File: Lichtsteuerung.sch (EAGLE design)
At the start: 154 parts, among them IC1 74HC595D, IC10 TSR_1-2450, IC11 MEGA64-A, IC12 75176AD, IC13 DS1307SO8, IC2 74HC595D, IC3 74HC595D, IC4 74HC595D, IC5 75176AD, IC6 MEGA8-AI, IC9 24FC128-I/SN, Q1 32.768, Q2 16MHz, Q3 16MHz, U1 MAX232SOIC16, X1 713-1410, X2 713-1410, X3 733-333, X5 713-1410, X6 733-334, X7 733-333, X8 733-333

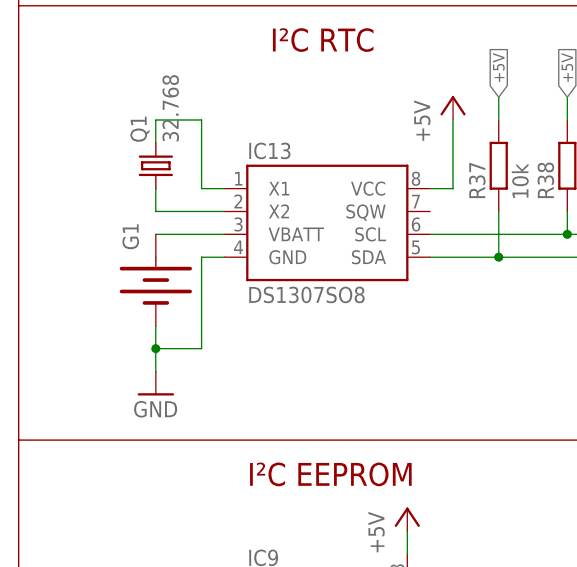
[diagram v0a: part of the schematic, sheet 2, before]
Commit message: Changed CR2032 battery holder with a vertical one to allow easier replacements
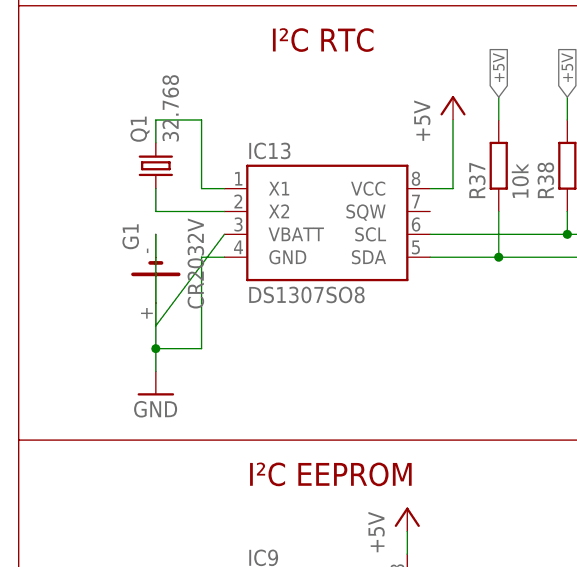
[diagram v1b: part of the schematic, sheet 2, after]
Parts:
- G1: value (none) -> CR2032V; device SparkFun:BATTERY20PTH -> cr2032v2:CR2032V
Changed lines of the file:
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@@
 <part name="FRAME3" library="frames" deviceset="A3L-LOC" device=""/>
 <part name="IC13" library="SparkFun" deviceset="DS1307" device="SO8"/>
-<part name="G1" library="SparkFun" deviceset="BATTERY" device="20PTH"/>
+<part name="G1" library="cr2032v2" deviceset="CR2032V" device=""/>
 <part name="Q1" library="crystal" deviceset="MC-306" device="" value="32.768"/>
 <part name="R37" library="resistor" deviceset="R-EU_" device="R0805" value="10k"/>
@@
 <instance part="FRAME3" gate="G$1" x="0" y="0"/>
 <instance part="IC13" gate="G$1" x="43.18" y="147.32"/>
-<instance part="G1" gate="G$1" x="25.4" y="139.7" smashed="yes" rot="R270">
+<instance part="G1" gate="1" x="25.4" y="139.7" smashed="yes" rot="R270">
 <attribute name="NAME" x="23.495" y="143.002" size="1.778" layer="95" rot="R90"/>
 <attribute name="VALUE" x="28.956" y="146.558" size="1.778" layer="96" rot="R270"/>
@@
 <net name="N$40" class="0">
 <segment>
-<wire x1="25.4" y1="144.78" x2="33.02" y2="144.78" width="0.1524" layer="91"/>
-<pinref part="G1" gate="G$1" pin="+"/>
+<wire x1="25.4" y1="134.62" x2="33.02" y2="144.78" width="0.1524" layer="91"/>
+<pinref part="G1" gate="1" pin="+"/>
 <pinref part="IC13" gate="G$1" pin="VBATT"/>
 </segment>
@@
 </segment>
 <segment>
-<wire x1="25.4" y1="134.62" x2="25.4" y2="132.08" width="0.1524" layer="91"/>
+<wire x1="25.4" y1="144.78" x2="25.4" y2="132.08" width="0.1524" layer="91"/>
 <wire x1="25.4" y1="132.08" x2="30.48" y2="132.08" width="0.1524" layer="91"/>
 <wire x1="30.48" y1="132.08" x2="30.48" y2="142.24" width="0.1524" layer="91"/>
@@
 <wire x1="25.4" y1="129.54" x2="25.4" y2="132.08" width="0.1524" layer="91"/>
 <junction x="25.4" y="132.08"/>
-<pinref part="G1" gate="G$1" pin="-"/>
+<pinref part="G1" gate="1" pin="-"/>
 <pinref part="IC13" gate="G$1" pin="GND"/>
 <pinref part="GND21" gate="1" pin="GND"/>

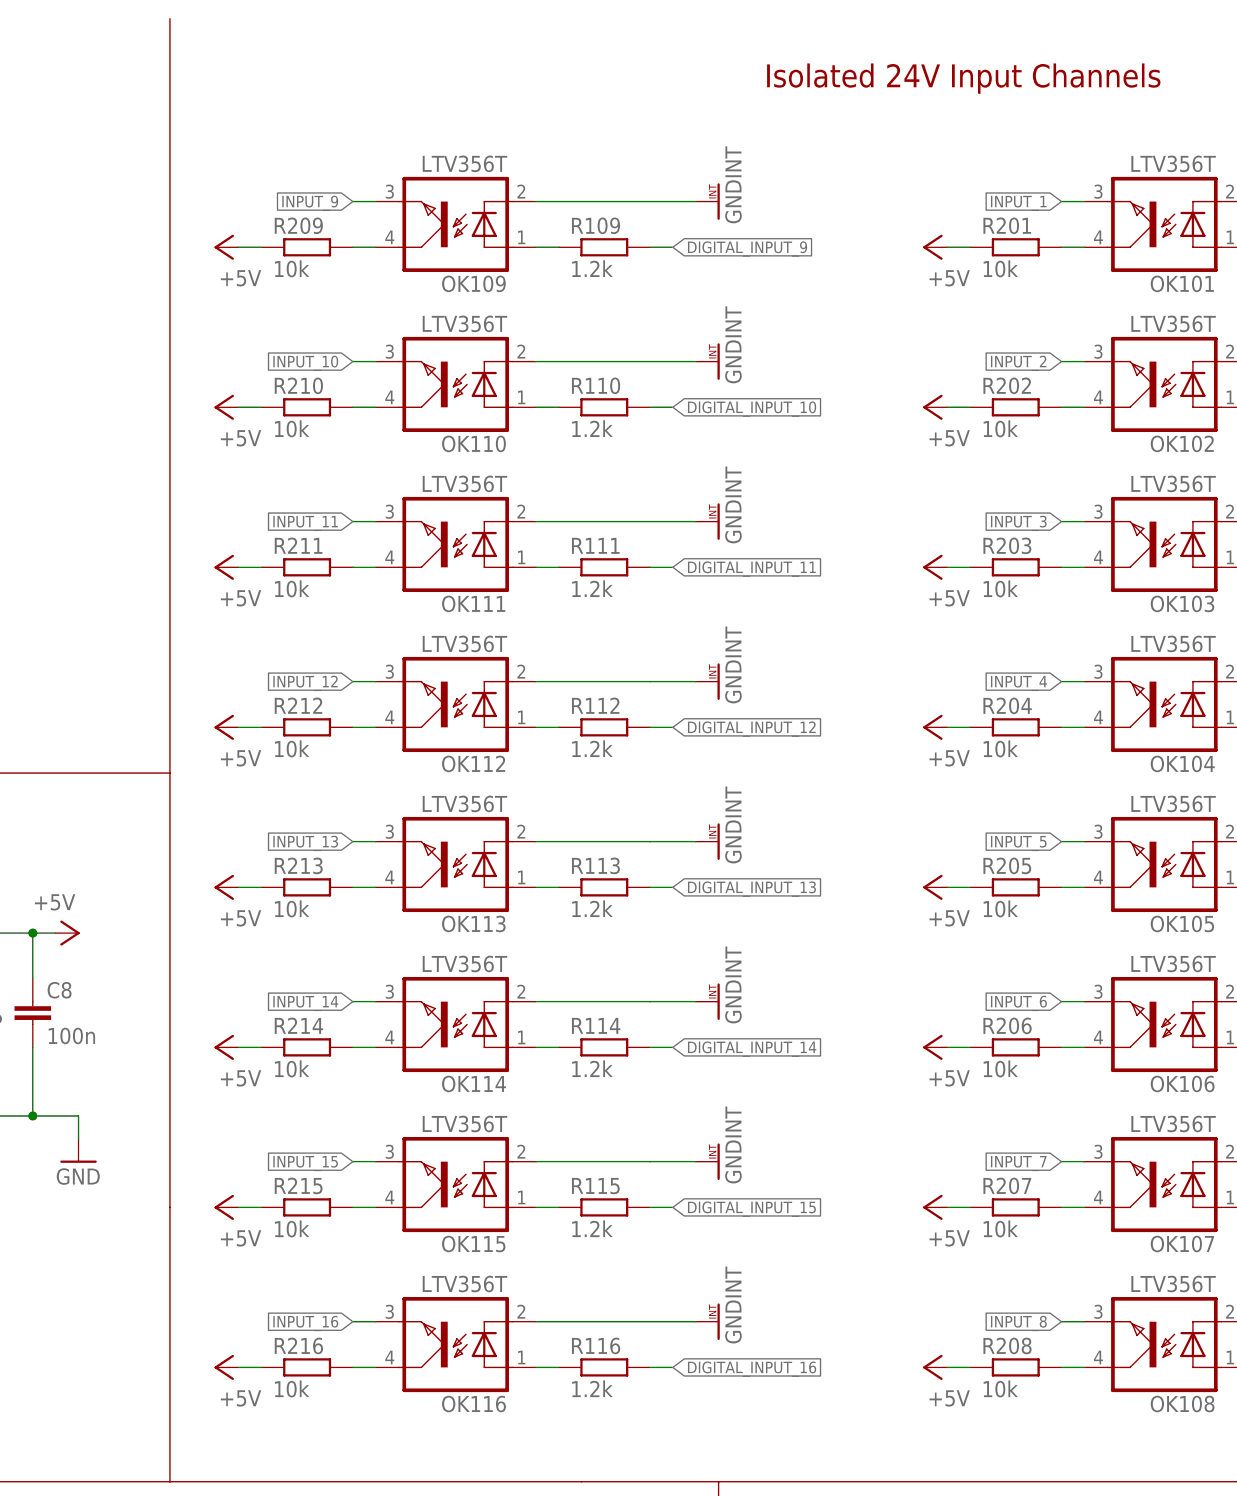
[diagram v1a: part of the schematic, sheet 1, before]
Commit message: Added missing pulldowns for the optocoupler inputs
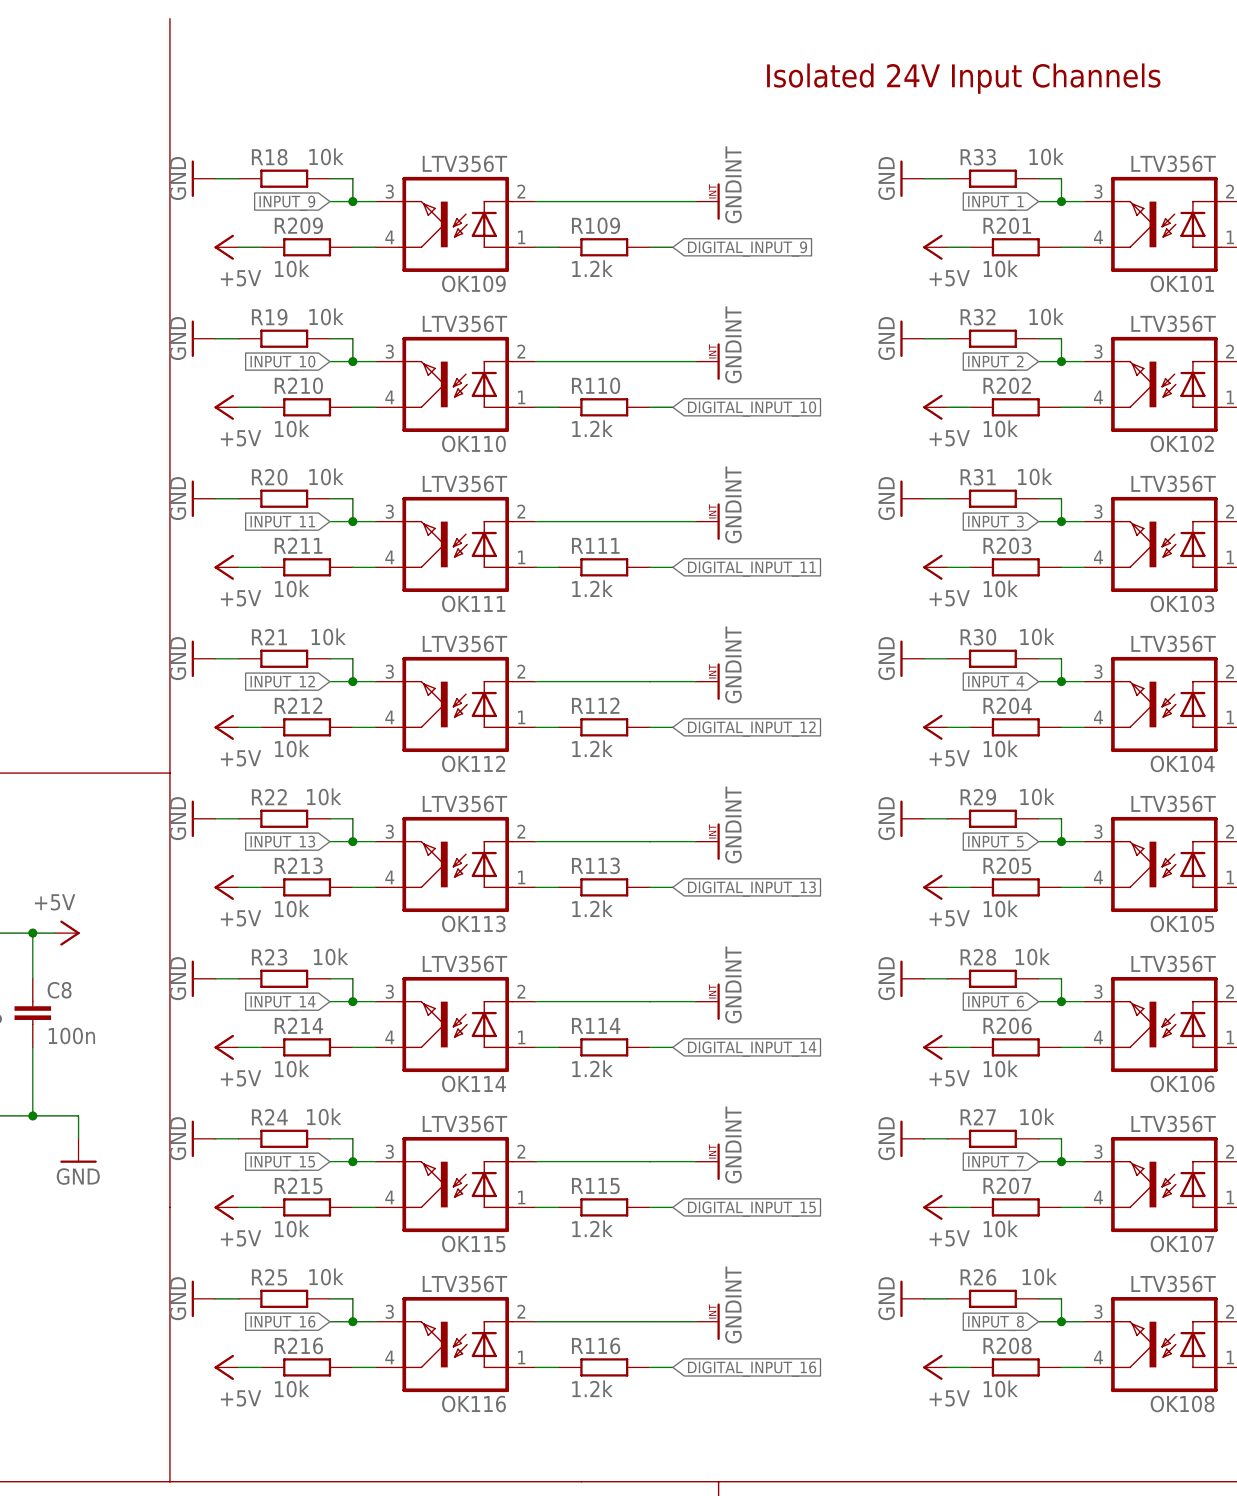
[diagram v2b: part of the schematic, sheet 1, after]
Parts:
- added R18, R19, R20, R21, R22, R23, R24, R25, R26, R27, R28, R29, R30, R31, R32, R33: 10k, resistor:R-EU_R0805
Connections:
- net GND: now also R18.1, R19.1, R20.1, R21.1, R22.1, R23.1, R24.1, R25.1, R26.1, R27.1, R28.1, R29.1, R30.1, R31.1, R32.1, R33.1
- net INPUT_1: now also R33.2
- net INPUT_10: now also R19.2
- net INPUT_11: now also R20.2
- net INPUT_12: now also R21.2
- net INPUT_13: now also R22.2
- net INPUT_14: now also R23.2
- net INPUT_15: now also R24.2
- net INPUT_16: now also R25.2
- net INPUT_2: now also R32.2
- net INPUT_3: now also R31.2
- net INPUT_4: now also R30.2
- net INPUT_5: now also R29.2
- net INPUT_6: now also R28.2
- net INPUT_7: now also R27.2
- net INPUT_8: now also R26.2
- net INPUT_9: now also R18.2
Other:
- moved on the sheet: G1

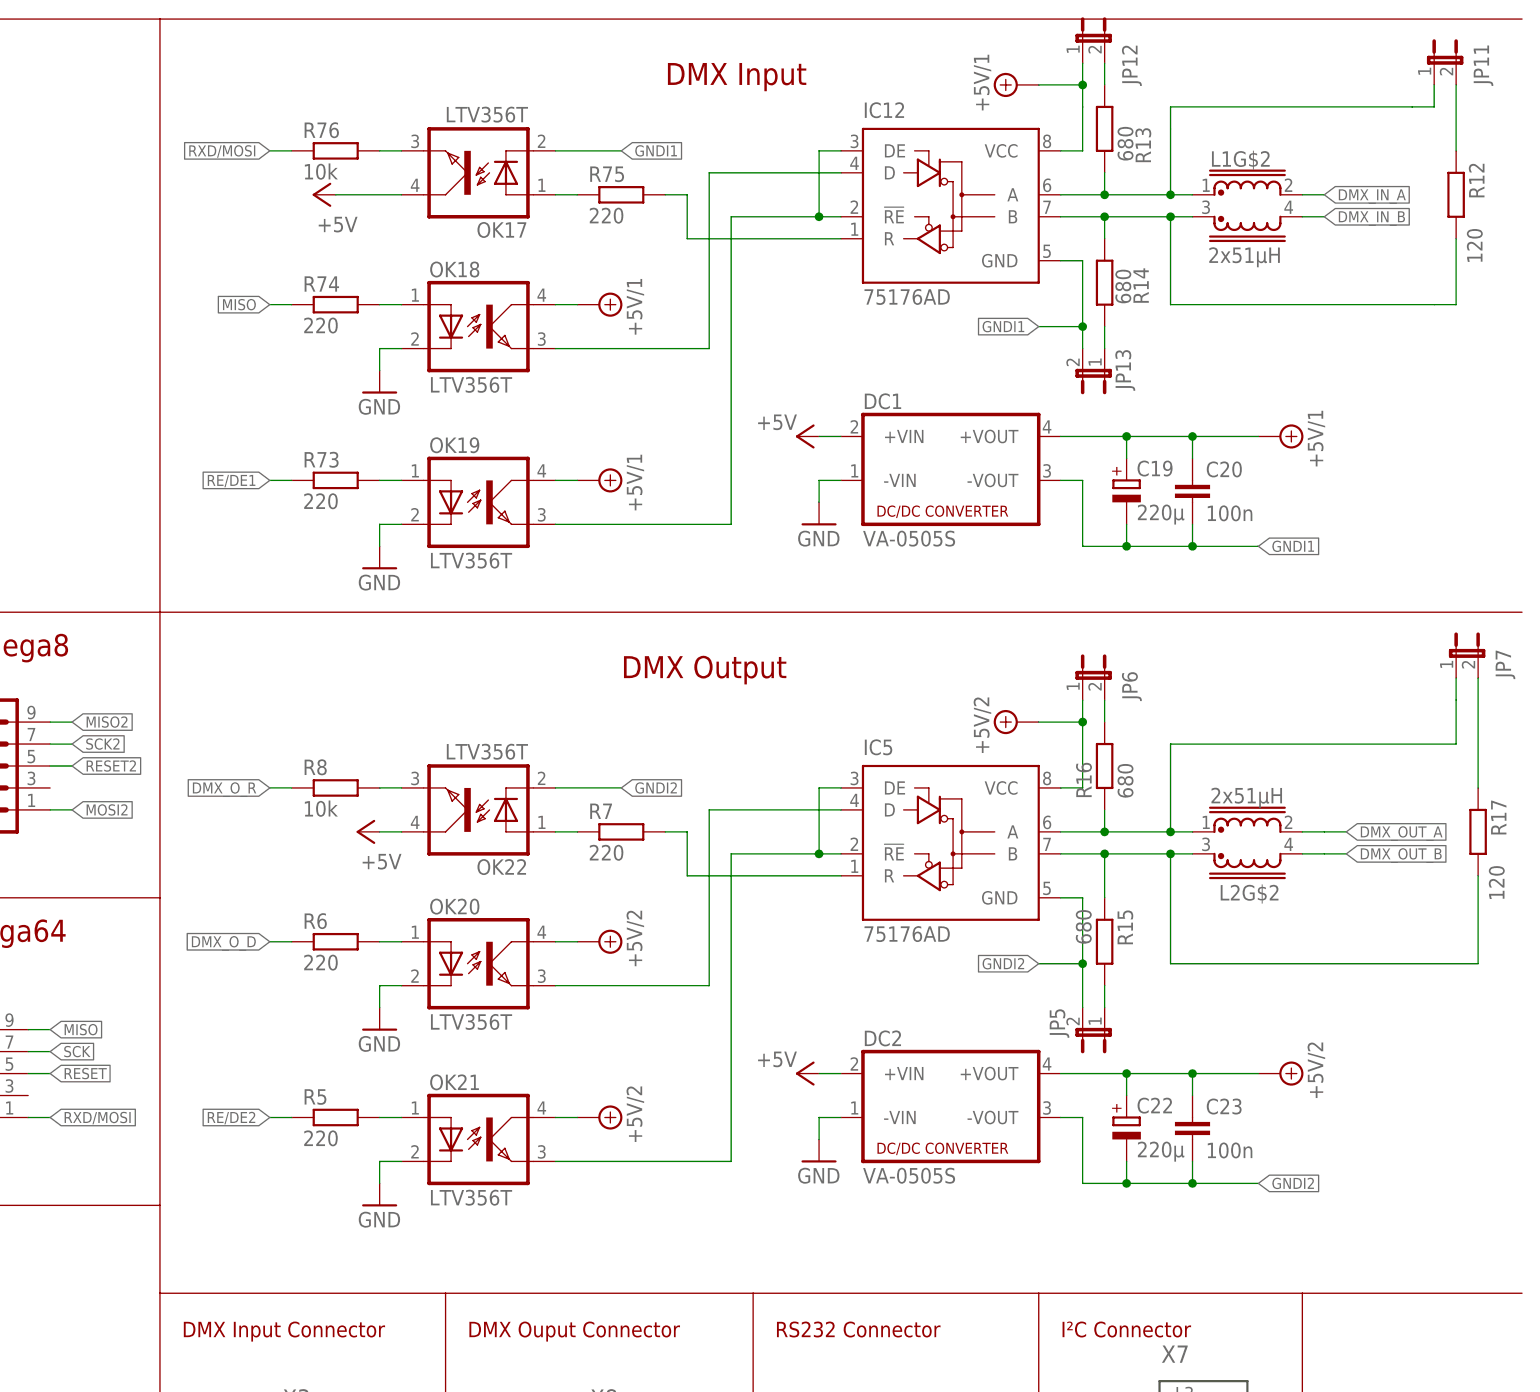
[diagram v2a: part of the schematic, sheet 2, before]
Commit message: Added new high-speed optocouplers
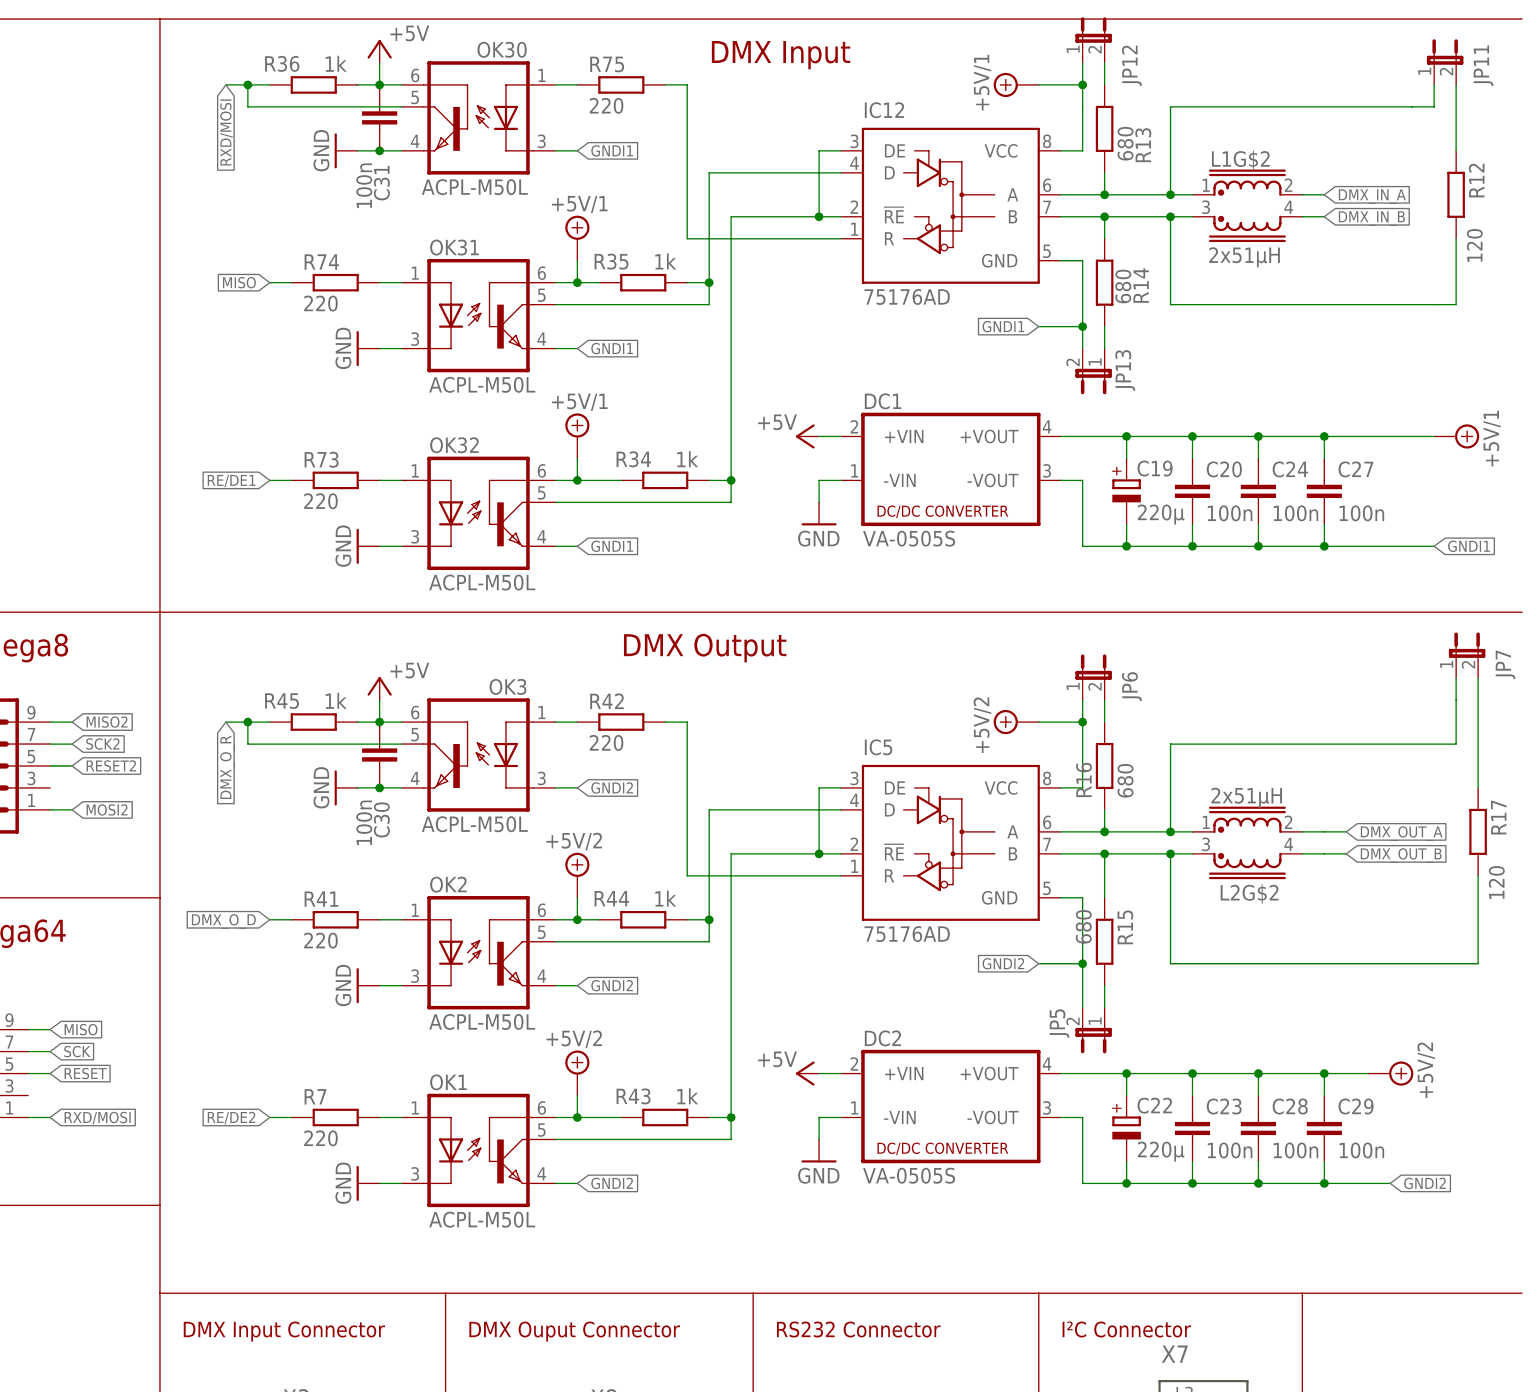
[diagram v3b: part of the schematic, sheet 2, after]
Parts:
- removed OK17, OK18, OK19, OK20, OK21, OK22: LTV356T, optocoupler:LTV816S
- removed R5, R6: 220, resistor:R-EU_R0805
- removed R76, R8: 10k, resistor:R-EU_R0805
- added C24, C27, C28, C29, C30, C31: 100n, rcl:C-EUC0805
- added OK1, OK2, OK3, OK30, OK31, OK32: ACPL-M50L, ACPL-M50L:ACPL-M50L
- added R34, R35, R36, R43, R44, R45: 1k, resistor:R-EU_R0805
- added R41, R42: 220, resistor:R-EU_R0805
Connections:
- removed net N$106: OK17.EMIT, R76.2
- removed net N$46: OK22.EMIT, R8.2
- removed net N$47: OK20.A, R6.2
- removed net N$48: OK21.A, R5.2
- removed net REC$2: IC5.R, R7.2
- removed net RE_OUT1: IC5.!RE, IC5.DE, OK21.EMIT
- removed net TXD_OUT1: IC5.D, OK20.EMIT
- new net N$73: OK2.A, R41.2
- new net N$79: OK1.A, R7.2
- new net REC$3: IC5.R, R42.2
- new net RE_OUT2: IC5.!RE, IC5.DE, OK1.COL, R43.1
- new net TXD_OUT2: IC5.D, OK2.COL, R44.1
- net +5V: now also C30.1, C31.1, OK3.BAS, OK30.BAS, R36.1, R45.1; no longer OK17.COL, OK22.COL
- net DMX_O_D: now also R41.1; no longer R6.1
- net DMX_O_R: now also OK3.COL, R45.2; no longer R8.1
- net GND: now also C30.2, C31.2, OK1.C, OK2.C, OK3.EMI, OK30.EMI, OK31.C, OK32.C; no longer OK18.C, OK19.C, OK20.C, OK21.C
- net GNDI1: now also C24.2, C27.2, OK30.C, OK31.EMI, OK32.EMI; no longer OK17.C
- net GNDI2: now also C28.2, C29.2, OK1.EMI, OK2.EMI, OK3.C; no longer OK22.C
- net N$104: now also OK30.A; no longer OK17.A
- net N$116: now also OK31.A; no longer OK18.A
- net N$133: now also OK32.A; no longer OK19.A
- net N$45: now also OK3.A, R42.1; no longer OK22.A, R7.1
- net RE/DE2: now also R7.1; no longer R5.1
- net RE_OUT: now also OK32.COL, R34.1; no longer OK19.EMIT
- net RXD/MOSI: now also OK30.COL, R36.2; no longer R76.1
- net TXD_OUT: now also OK31.COL, R35.1; no longer OK18.EMIT
- net VCCIO1: now also C24.1, C27.1, OK31.BAS, OK32.BAS, R34.2, R35.2; no longer OK18.COL, OK19.COL
- net VCCIO2: now also C28.1, C29.1, OK1.BAS, OK2.BAS, R43.2, R44.2; no longer OK20.COL, OK21.COL
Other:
- moved on the sheet: R7, R74, R75
